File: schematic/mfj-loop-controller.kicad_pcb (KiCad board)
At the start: 2 copper layers, 191.8 x 101.6 mm, 29 parts, among them J1 Bias Tee, J2 +12VDC, J3 SWR Bridge, J4 Conn_01x10_Female, U1 TMR9-1212, U2 R-785.0-1.0, U3 LCC120, U4 LCC120, U5 LCC120, U6 LCC120, U7 WeMos_D1_mini

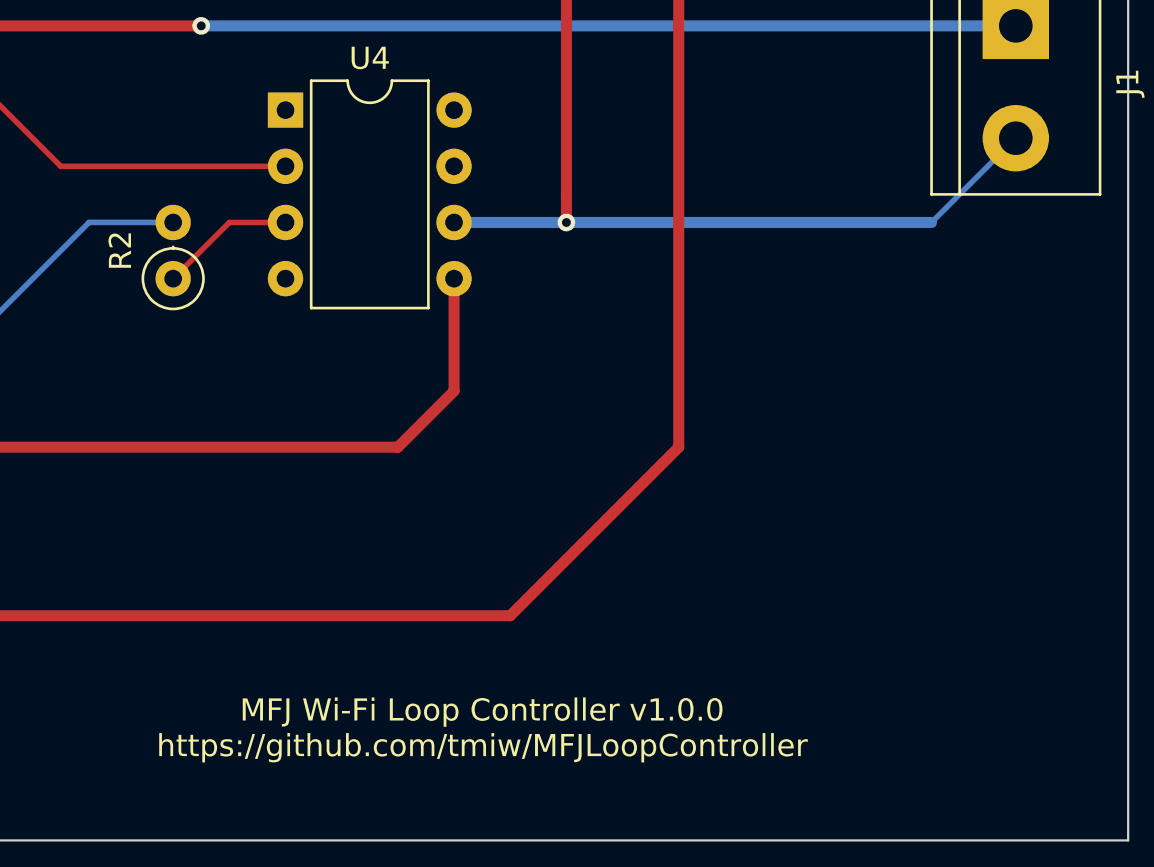
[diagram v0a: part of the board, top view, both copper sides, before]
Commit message: Update PCB markings and version info.
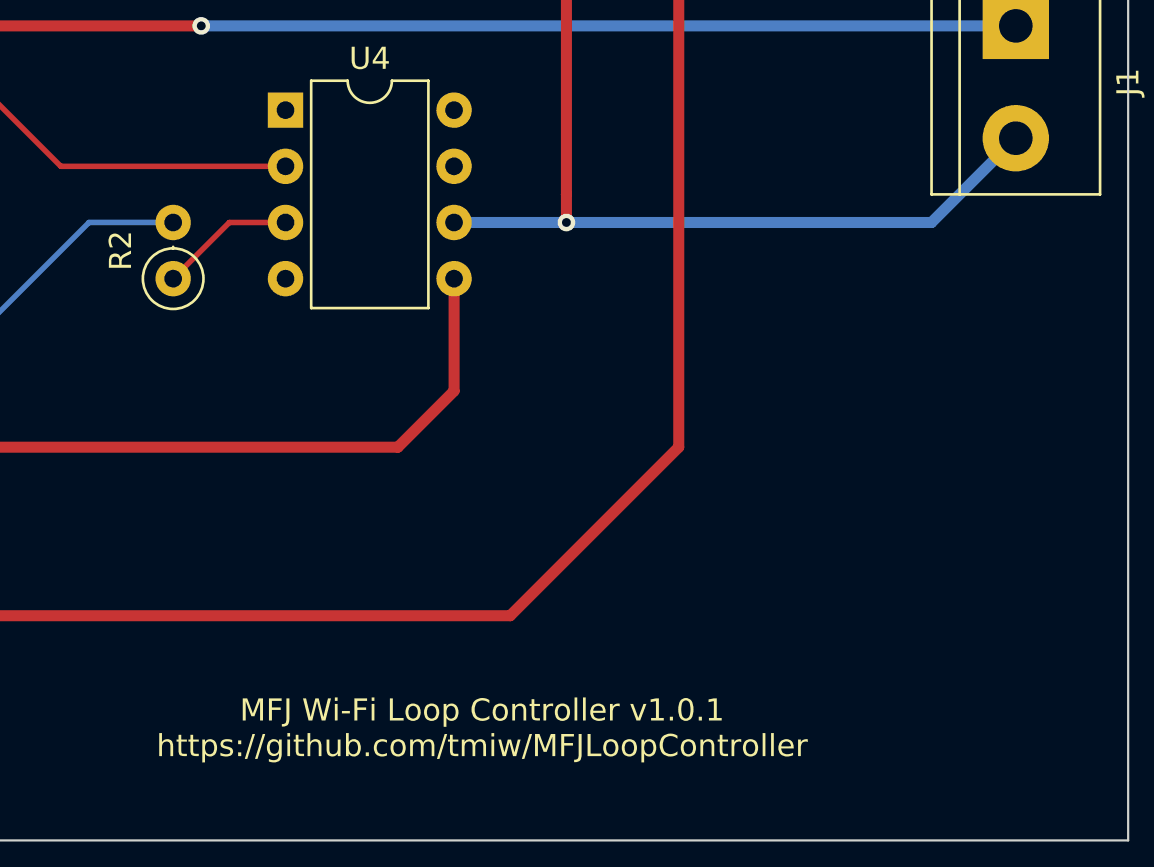
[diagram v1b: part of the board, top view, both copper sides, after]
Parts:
- J4: value Conn_01x10_Female -> Adafruit ADS1115
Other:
- board text added: "MFJ Wi-Fi Loop Controller v1.0.1 https://github.com/tmiw/MFJLoopController"
- board text removed: "MFJ Wi-Fi Loop Controller v1.0.0 https://github.com/tmiw/MFJLoopController"

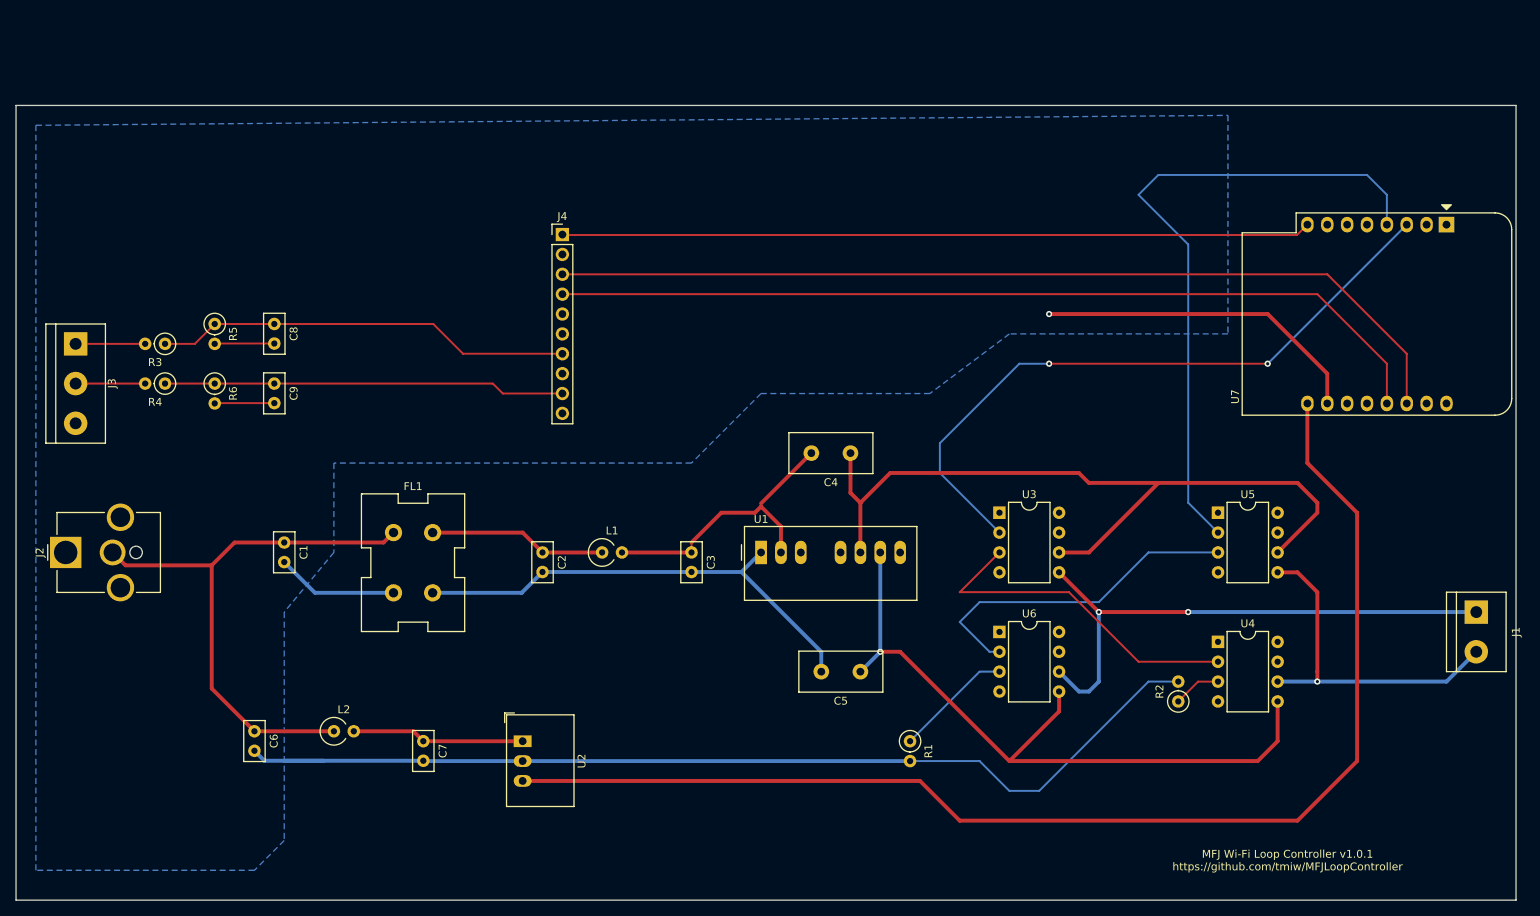
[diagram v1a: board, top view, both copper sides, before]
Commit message: Update schematic and PCB to v1.1.0:
1. Shrink board footprint to ~4x3" for ease of mounting/EMI compliance.
2. Add mounting holes to corners.
3. Add GND/+12V flood fill layers for EMI compliance/routing.
4. Increase size of R/C/L component footprints for ease of assembly.
5. Add route for ADC alert pin to ESP82xx board.
6. Add routes for ADC analog negative pins to ground.
7. Add buffer op-amp + supporting RC filters in front of ADC.
8. Add Open Hardware logo to silkscreen.
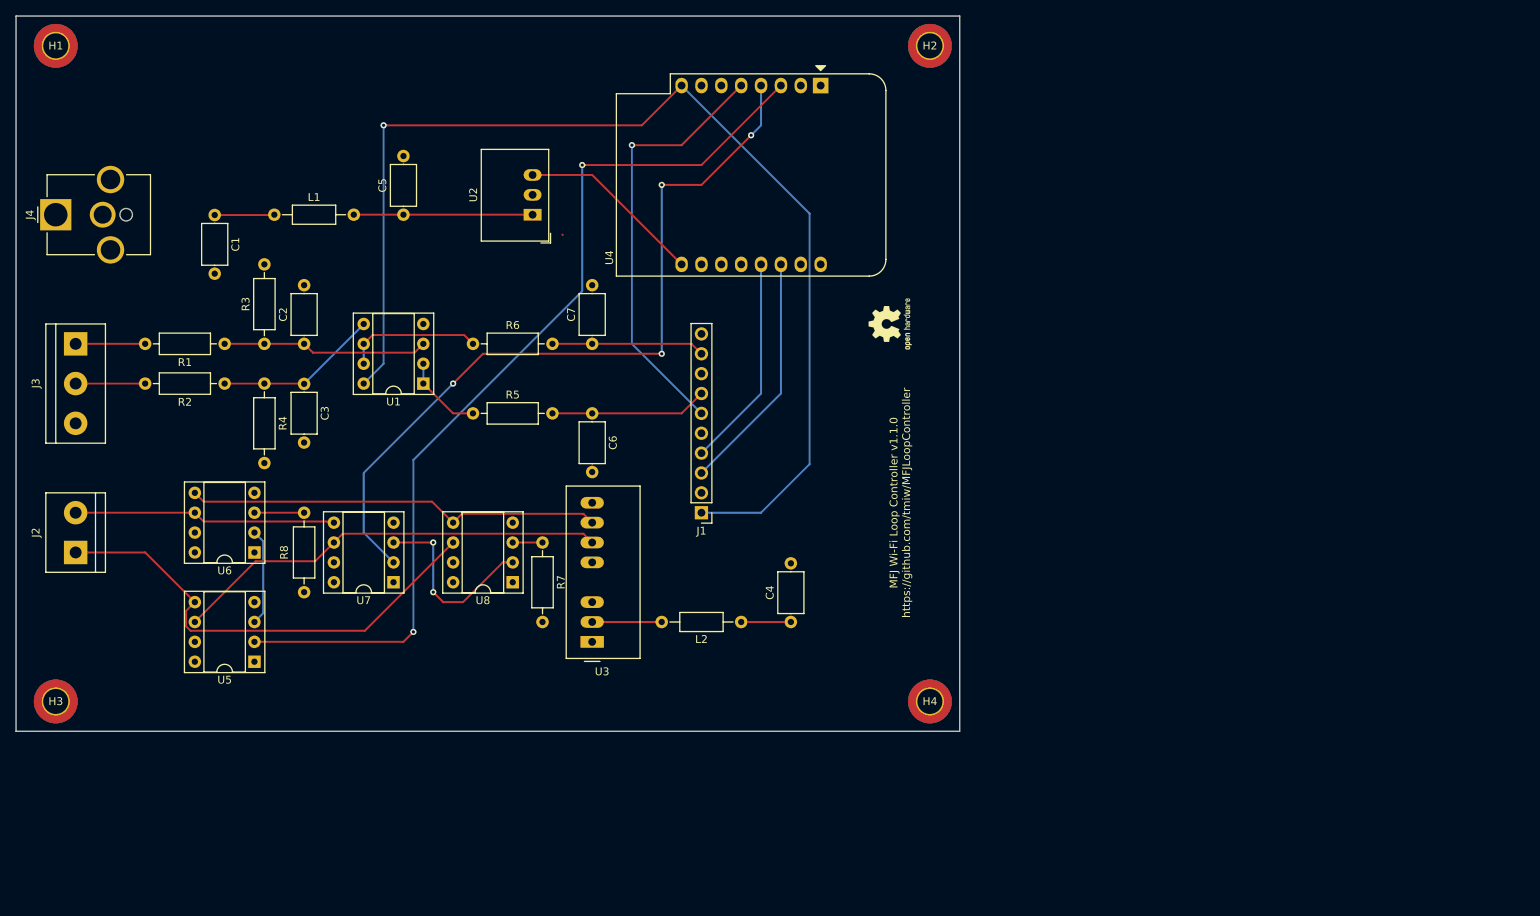
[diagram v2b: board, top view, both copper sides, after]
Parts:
- removed C8, C9: 4.7nF, Capacitor_THT:C_Disc_D5.0mm_W2.5mm_P2.50mm
- removed FL1: 7448421016, Inductor_THT:L_CommonMode_Wuerth_WE-CMB-S
- added H1: MountingHole_Pad, MountingHole:MountingHole_3.2mm_M3_DIN965_Pad_TopBottom, F.Cu at (63.5, 29.2)
- added H2: MountingHole_Pad, MountingHole:MountingHole_3.2mm_M3_DIN965_Pad_TopBottom, F.Cu at (175.3, 29.2)
- added H3: MountingHole_Pad, MountingHole:MountingHole_3.2mm_M3_DIN965_Pad_TopBottom, F.Cu at (63.5, 113.0)
- added H4: MountingHole_Pad, MountingHole:MountingHole_3.2mm_M3_DIN965_Pad_TopBottom, F.Cu at (175.3, 113.0)
- added R7: 100, Resistor_THT:R_Axial_DIN0207_L6.3mm_D2.5mm_P10.16mm_Horizontal, F.Cu at (125.7, 92.7)
- added R8: 100, Resistor_THT:R_Axial_DIN0207_L6.3mm_D2.5mm_P10.16mm_Horizontal, F.Cu at (95.2, 88.9)
- added REF**: OSHW-Logo2_7.3x6mm_SilkScreen, Symbol:OSHW-Logo2_7.3x6mm_SilkScreen, F.Cu at (170.2, 64.8)
- added U8: LCC120, Package_DIP:DIP-8_W7.62mm_Socket, F.Cu at (121.9, 97.8)
- C1: value 10uF 50V -> 10uF 100V; footprint Capacitor_THT:C_Disc_D5.0mm_W2.5mm_P2.50mm -> Capacitor_THT:C_Axial_L5.1mm_D3.1mm_P7.50mm_Horizontal
- C2, C3: value 10uF 50V -> 4.7nF; footprint Capacitor_THT:C_Disc_D5.0mm_W2.5mm_P2.50mm -> Capacitor_THT:C_Axial_L5.1mm_D3.1mm_P7.50mm_Horizontal
- C4: value 220pF 2000V -> 2.2uF 25V; footprint Capacitor_THT:C_Disc_D10.5mm_W5.0mm_P5.00mm -> Capacitor_THT:C_Axial_L5.1mm_D3.1mm_P7.50mm_Horizontal
- C5: value 220pF 2000V -> 2.2uF 100V; footprint Capacitor_THT:C_Disc_D10.5mm_W5.0mm_P5.00mm -> Capacitor_THT:C_Axial_L5.1mm_D3.1mm_P7.50mm_Horizontal
- C6: value 10uF 100V -> 2.2uF; footprint Capacitor_THT:C_Disc_D5.0mm_W2.5mm_P2.50mm -> Capacitor_THT:C_Axial_L5.1mm_D3.1mm_P7.50mm_Horizontal
- C7: value 2.2uF 100V -> 2.2uF; footprint Capacitor_THT:C_Disc_D5.0mm_W2.5mm_P2.50mm -> Capacitor_THT:C_Axial_L5.1mm_D3.1mm_P7.50mm_Horizontal
- J1: value Bias Tee -> Adafruit ADS1115; footprint TerminalBlock:TerminalBlock_bornier-2_P5.08mm -> Connector_PinHeader_2.54mm:PinHeader_1x10_P2.54mm_Vertical
- J2: value +12VDC -> Bias Tee; footprint Connector_BarrelJack:BarrelJack_CUI_PJ-063AH_Horizontal_CircularHoles -> TerminalBlock:TerminalBlock_bornier-2_P5.08mm
- J4: value Adafruit ADS1115 -> DC+12V; footprint Connector_PinHeader_2.54mm:PinHeader_1x10_P2.54mm_Vertical -> Connector_BarrelJack:BarrelJack_CUI_PJ-063AH_Horizontal_CircularHoles
- L1: value 10uH -> 5.6uH; footprint Inductor_THT:L_Axial_L7.0mm_D3.3mm_P2.54mm_Vertical_Fastron_MICC -> Inductor_THT:L_Axial_L5.3mm_D2.2mm_P10.16mm_Horizontal_Vishay_IM-1
- L2: value 5.6uH -> 18uH; footprint Inductor_THT:L_Axial_L7.0mm_D3.3mm_P2.54mm_Vertical_Fastron_MICC -> Inductor_THT:L_Axial_L5.3mm_D2.2mm_P10.16mm_Horizontal_Vishay_IM-1
- R1, R2: value 100 -> 22K; footprint Resistor_THT:R_Axial_DIN0207_L6.3mm_D2.5mm_P2.54mm_Vertical -> Resistor_THT:R_Axial_DIN0207_L6.3mm_D2.5mm_P10.16mm_Horizontal
- R3, R4: value 22K -> 18K; footprint Resistor_THT:R_Axial_DIN0207_L6.3mm_D2.5mm_P2.54mm_Vertical -> Resistor_THT:R_Axial_DIN0207_L6.3mm_D2.5mm_P10.16mm_Horizontal
- R5, R6: value 18K -> 150; footprint Resistor_THT:R_Axial_DIN0207_L6.3mm_D2.5mm_P2.54mm_Vertical -> Resistor_THT:R_Axial_DIN0207_L6.3mm_D2.5mm_P10.16mm_Horizontal
- U1: value TMR9-1212 -> AD8032; footprint Converter_DCDC:Converter_DCDC_TRACO_TMR-xxxx_THT -> Package_DIP:DIP-8_W7.62mm_Socket
- U3: value LCC120 -> TMR3-1212; footprint Package_DIP:DIP-8_W7.62mm -> Converter_DCDC:Converter_DCDC_TRACO_TMR-xxxx_THT
- U4: value LCC120 -> WeMos_D1_mini; footprint Package_DIP:DIP-8_W7.62mm -> Module:WEMOS_D1_mini_light
- U5, U6: footprint Package_DIP:DIP-8_W7.62mm -> Package_DIP:DIP-8_W7.62mm_Socket
- U7: value WeMos_D1_mini -> LCC120; footprint Module:WEMOS_D1_mini_light -> Package_DIP:DIP-8_W7.62mm_Socket
- moved U7 142.2 mm to (106.7, 97.8), turned to 180 degrees
- moved R2 128.5 mm to (85.1, 72.4), turned to 180 degrees
- moved U5 124.7 mm to (88.9, 108.0), turned to 180 degrees
- moved R1 101.3 mm to (85.1, 67.3), turned to 180 degrees
- moved J1 99.9 mm to (146.1, 88.9), turned to 180 degrees
- moved U6 95.8 mm to (88.9, 94.0), turned to 180 degrees
- moved U4 87.4 mm to (161.3, 34.3), turned to 270 degrees
- moved C5 82.6 mm to (108.0, 50.8), turned to 90 degrees
- moved U2 67.3 mm to (124.5, 50.8), turned to 90 degrees
- moved J4 64.8 mm to (63.5, 50.8), turned to 90 degrees
- moved L1 60.2 mm to (91.4, 50.8)
- moved C6 59.3 mm to (132.1, 76.2)
- moved C7 55.2 mm to (132.1, 67.3), turned to 90 degrees
- moved U3 54.6 mm to (132.1, 105.4), turned to 90 degrees
- moved C3 54.0 mm to (95.2, 72.4)
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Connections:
- C2 pad 2: Net-(C2-Pad2) -> GND
- C3 pad 2: Net-(C2-Pad2) -> GND
- C4 pad 1: /ISOLATED_12V -> +12V
- C4 pad 2: Net-(C3-Pad1) -> GND
- C5 pad 1: /ISOLATED_GND -> Net-(C5-Pad1)
- C5 pad 2: Net-(C2-Pad2) -> GND
- C6 pad 1: +12V -> Net-(C6-Pad1)
- J1 pad 1: /BIAS_L -> /POWER_3.3V
- J1 pad 2: /BIAS_R -> GND
- J2 pad 1: GND -> /BIAS_L
- J2 pad 2: +12V -> /BIAS_R
- J4 pad 1: /POWER_3.3V -> GND
- J4 pad 2: GND -> +12V
- L1 pad 1: Net-(C2-Pad1) -> +12V
- L1 pad 2: Net-(C3-Pad1) -> Net-(C5-Pad1)
- L2 pad 2: Net-(C7-Pad1) -> Net-(L2-Pad2)
- R1 pad 1: Net-(R1-Pad1) -> Net-(C2-Pad1)
- R1 pad 2: GND -> /FWD_POWER
- R2 pad 1: Net-(R2-Pad1) -> Net-(C3-Pad1)
- R2 pad 2: GND -> /REV_PWR
- R3 pad 1: Net-(C8-Pad1) -> Net-(C2-Pad1)
- R3 pad 2: /FWD_POWER -> GND
- R4 pad 1: Net-(C9-Pad1) -> Net-(C3-Pad1)
- R4 pad 2: /REV_PWR -> GND
- R5 pad 1: Net-(C8-Pad1) -> Net-(R5-Pad1)
- R5 pad 2: GND -> Net-(C6-Pad1)
- R6 pad 1: Net-(C9-Pad1) -> Net-(R6-Pad1)
- R6 pad 2: GND -> Net-(C7-Pad1)
- U1 pad 1: Net-(C2-Pad2) -> Net-(R5-Pad1)
- U1 pad 2: Net-(C3-Pad1) -> Net-(R5-Pad1)
- U1 pad 3: Net-(U1-Pad3) -> Net-(C2-Pad1)
- U1 pad 5: Net-(U1-Pad5) -> Net-(C3-Pad1)
- U1 pad 6: /ISOLATED_12V -> Net-(R6-Pad1)
- U1 pad 7: /ISOLATED_GND -> Net-(R6-Pad1)
- U1 pad 8: Net-(U1-Pad8) -> /POWER_3.3V
- U2 pad 1: Net-(C7-Pad1) -> Net-(C5-Pad1)
- U3 pad 1: Net-(U3-Pad1) -> GND
- U3 pad 2: /GPIO_TUNE_UP -> Net-(L2-Pad2)
- U3 pad 5: /BIAS_L -> Net-(U3-Pad5)
- U3 pad 7: Net-(U3-Pad7) -> /ISOLATED_GND
- U4 pad 2: Net-(U3-Pad3) -> Net-(U4-Pad2)
- U4 pad 3: Net-(R2-Pad1) -> /GPIO_TUNE_UP
- U4 pad 4: Net-(U4-Pad4) -> /GPIO_TUNE_DOWN
- U4 pad 5: /ISOLATED_GND -> /ADC_ALERT
- U4 pad 6: /BIAS_R -> Net-(U4-Pad6)
- U4 pad 8: Net-(U4-Pad8) -> /POWER_3.3V
- U5 pad 2: /GPIO_TUNE_DOWN -> /GPIO_TUNE_UP
- U5 pad 5: /BIAS_R -> /BIAS_L
- U6 pad 3: Net-(R1-Pad1) -> Net-(R8-Pad1)
- U6 pad 6: /BIAS_L -> /BIAS_R
- U7 pad 2: Net-(U7-Pad2) -> /GPIO_TUNE_DOWN
- U7 pad 3: /GPIO_TUNE_UP -> Net-(U7-Pad3)
- U7 pad 4: /GPIO_TUNE_DOWN -> Net-(U7-Pad4)
- U7 pad 5: Net-(U7-Pad5) -> /BIAS_R
- U7 pad 6: Net-(U7-Pad6) -> /ISOLATED_12V
- U7 pad 8: /POWER_3.3V -> Net-(U7-Pad8)
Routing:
- net GND: track 204.6 -> 0.08 mm, vias 1 -> 0
- net /POWER_5V: track 160.3 -> 23.8 mm
- net /ADC_SCL: track 118.5 -> 30.9 mm
- net /ADC_SDA: track 114.2 -> 27.3 mm
- net Net-(C2-Pad2): track 61.1 -> 0.00 mm
- net +12V: track 72.0 -> 14.0 mm
- net /ADC_ALERT: track 0.00 -> 55.1 mm, vias 0 -> 1
- net Net-(C8-Pad1): track 53.4 -> 0.00 mm
- net Net-(C9-Pad1): track 51.3 -> 0.00 mm
- net /POWER_3.3V: track 95.8 -> 145.9 mm, vias 0 -> 1
- net Net-(U3-Pad3): track 43.9 -> 0.00 mm
- net /ISOLATED_12V: track 99.6 -> 55.9 mm
- net /ISOLATED_GND: track 90.5 -> 53.3 mm, vias 1 -> 0
- net /GPIO_TUNE_UP: track 85.8 -> 119.1 mm
- net Net-(U5-Pad3): track 43.4 -> 12.4 mm
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- added copper zone on In2.Cu, net +12V
- added copper zone on In1.Cu, net GND
- removed copper zone on B.Cu, net GND
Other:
- board size 191.8 x 101.6 mm -> 120.6 x 91.4 mm
- copper layers 2 -> 4
- board text added: "MFJ Wi-Fi Loop Controller v1.1.0 https://github.com/tmiw/MFJLoopController"
- board text removed: "MFJ Wi-Fi Loop Controller v1.0.1 https://github.com/tmiw/MFJLoopController"

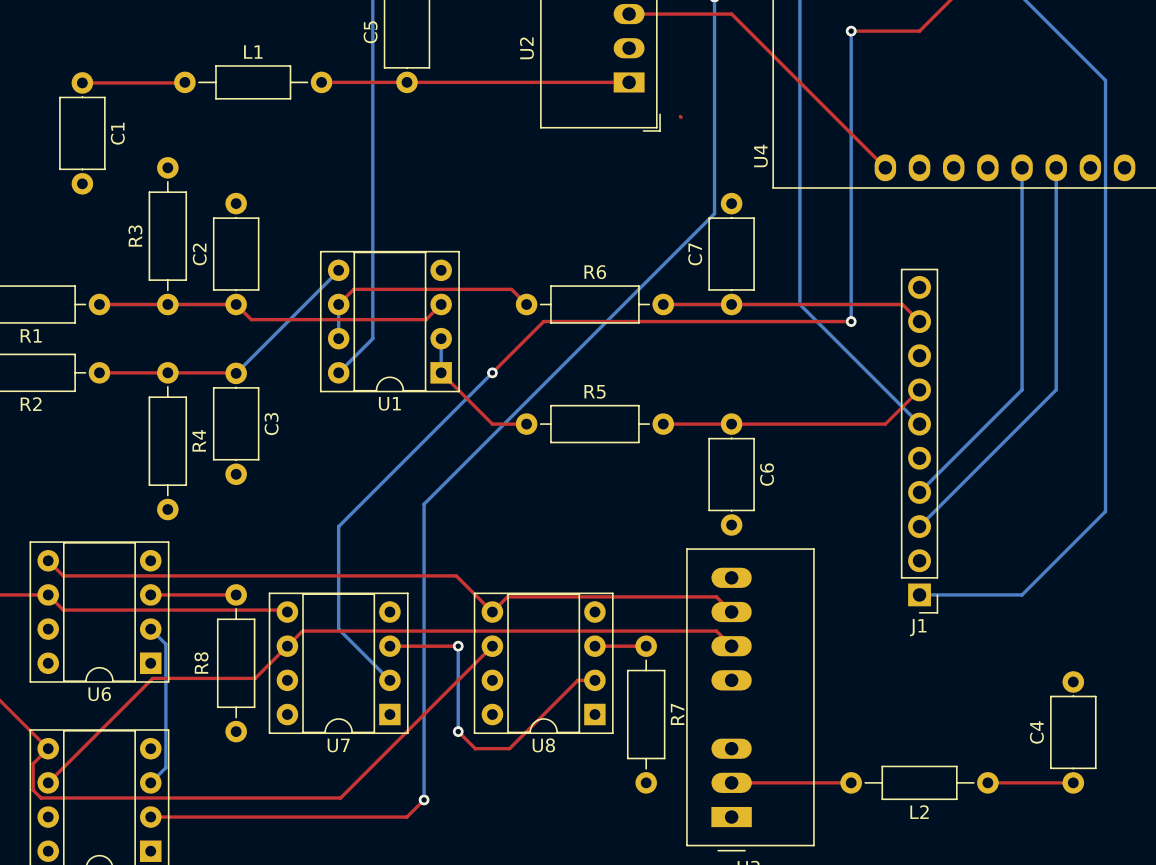
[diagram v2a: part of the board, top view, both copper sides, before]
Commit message: Update design rules.
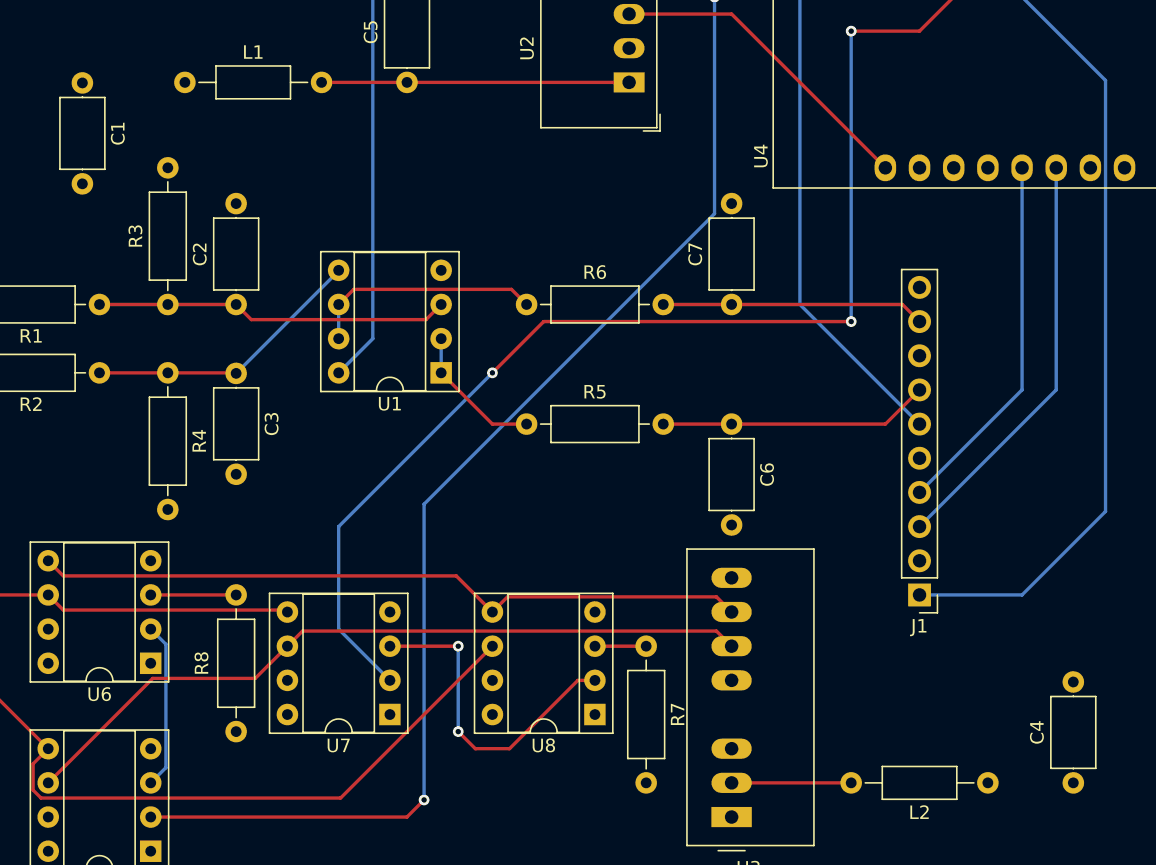
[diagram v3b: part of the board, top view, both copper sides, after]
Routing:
- net +12V: track 14.0 -> 0.06 mm
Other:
- net class Default: trace_width 0.25 -> 0.127; via_dia 0.8 -> 0.4572; via_drill 0.4 -> 0.254
- rule pad_to_mask_clearance: 0 -> 0.0508
- rule trace_min: 0.2 -> 0.127
- rule via_min_drill: 0.3 -> 0.254
- rule via_min_size: 0.4 -> 0.4572
